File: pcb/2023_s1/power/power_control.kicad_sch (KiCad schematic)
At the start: 21 parts, among them J1 Conn_01x05_Male, Q2 TIP122, U1 40106, U3 4N25

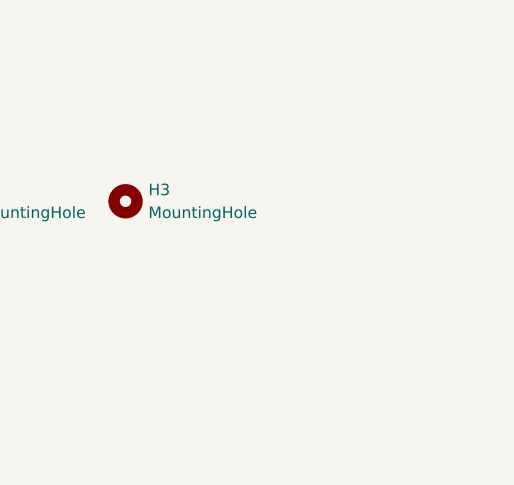
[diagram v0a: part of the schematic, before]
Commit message: fix, added a 4th mounting hole and rerouted the pcb in order to make feasible to solder given our poor infrastructure for PCB production
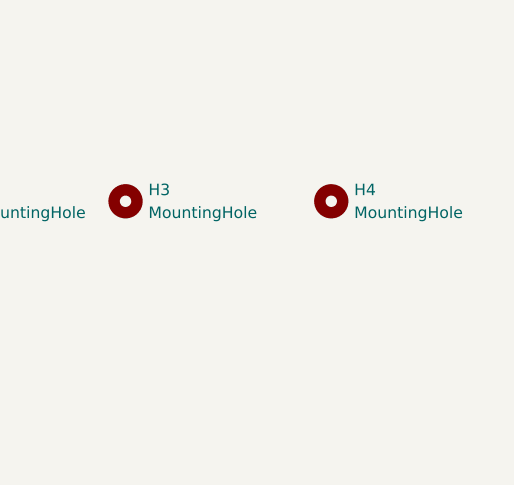
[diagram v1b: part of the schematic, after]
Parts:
- added H4: MountingHole, MountingHole:MountingHole_3.2mm_M3_DIN965_Pad, symbol Mechanical:MountingHole
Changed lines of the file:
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@@
     (pin "3")
+  )
+  (symbol (lib_id "Mechanical:MountingHole") (at 204.47 33.02 0) (unit 1)
+    (in_bom yes) (on_board yes) (fields_autoplaced)
+    (property "Reference" "H4" (id 0) (at 207.01 31.7499 0)
+      (effects (font (size 1.27 1.27)) (justify left))
+    )
+    (property "Value" "MountingHole" (id 1) (at 207.01 34.2899 0)
+      (effects (font (size 1.27 1.27)) (justify left))
+    )
+    (property "Footprint" "MountingHole:MountingHole_3.2mm_M3_DIN965_Pad" (id 2) (at 204.47 33.02 0)
+      (effects (font (size 1.27 1.27)) hide)
+    )
+    (property "Datasheet" "~" (id 3) (at 204.47 33.02 0)
+      (effects (font (size 1.27 1.27)) hide)
+    )
   )
   (symbol (lib_id "Connector:Screw_Terminal_01x02") (at 94.996 41.021 0) (unit 1)
@@
       (reference "H3") (unit 1) (value "MountingHole") (footprint "MountingHole:MountingHole_3.2mm_M3_DIN965_Pad")
     )
+    (path "/613046ba-2470-4560-9474-2ccc8166422c"
+      (reference "H4") (unit 1) (value "MountingHole") (footprint "MountingHole:MountingHole_3.2mm_M3_DIN965_Pad")
+    )
     (path "/656d544d-84ad-4bbf-8e72-6258e93c8b6e"

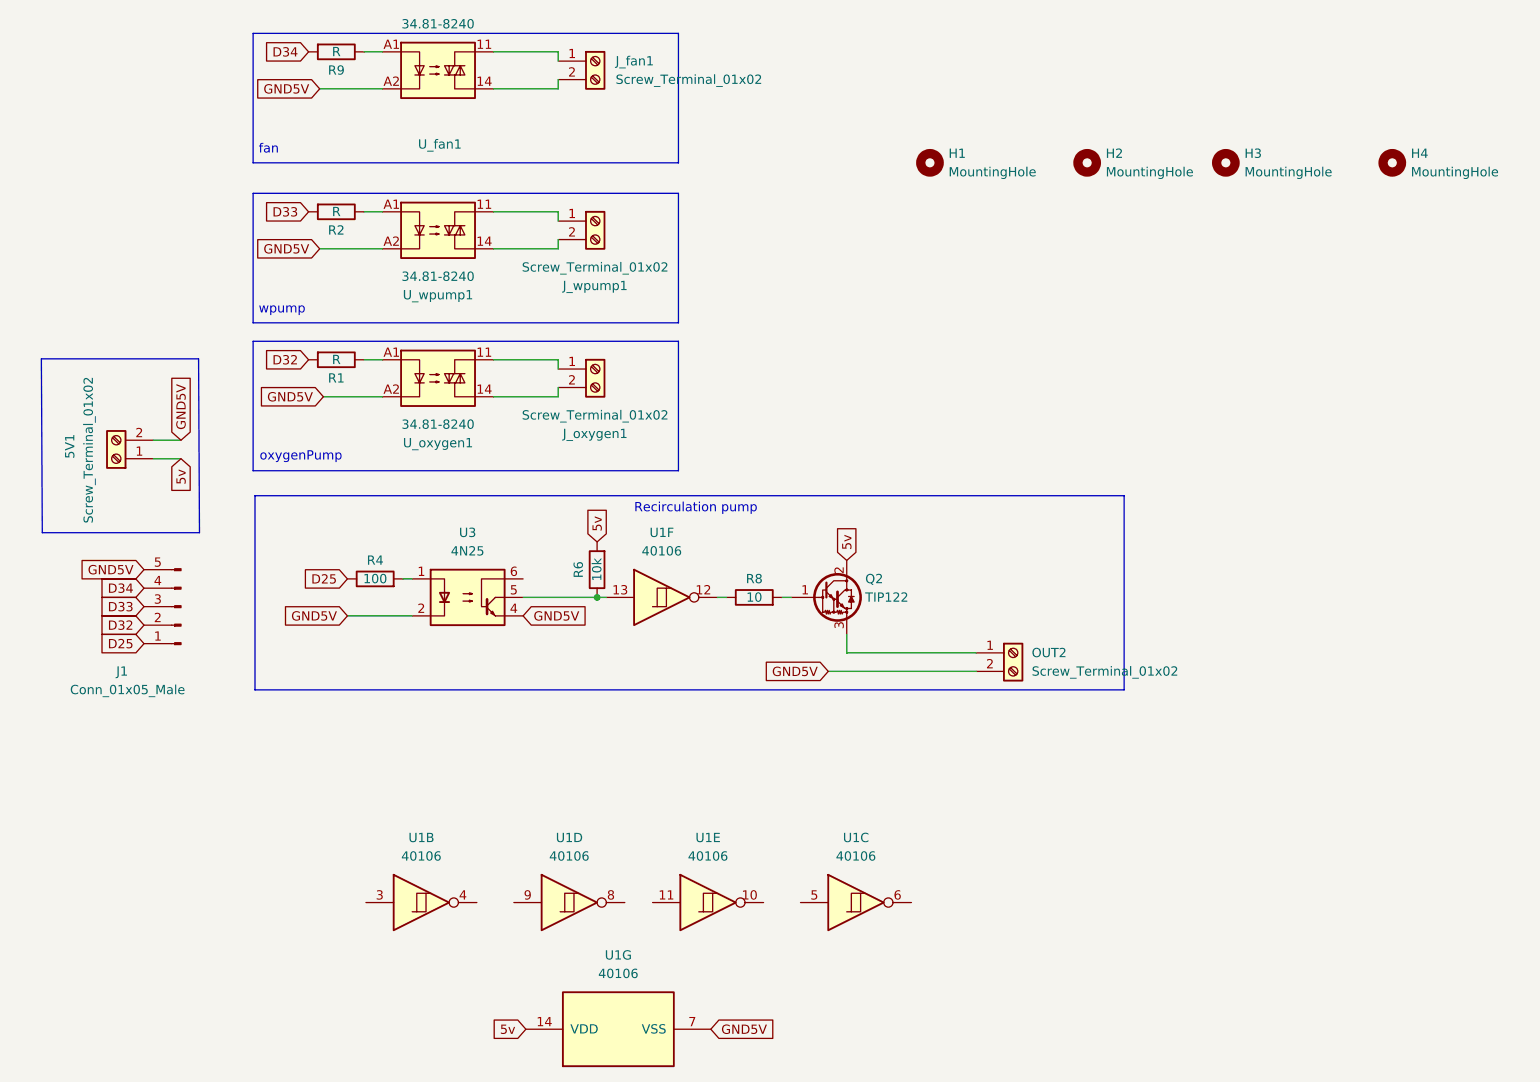
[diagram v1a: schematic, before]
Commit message: update, reselection of output pins and ds18b20 pin, rerouting and resizing of pads
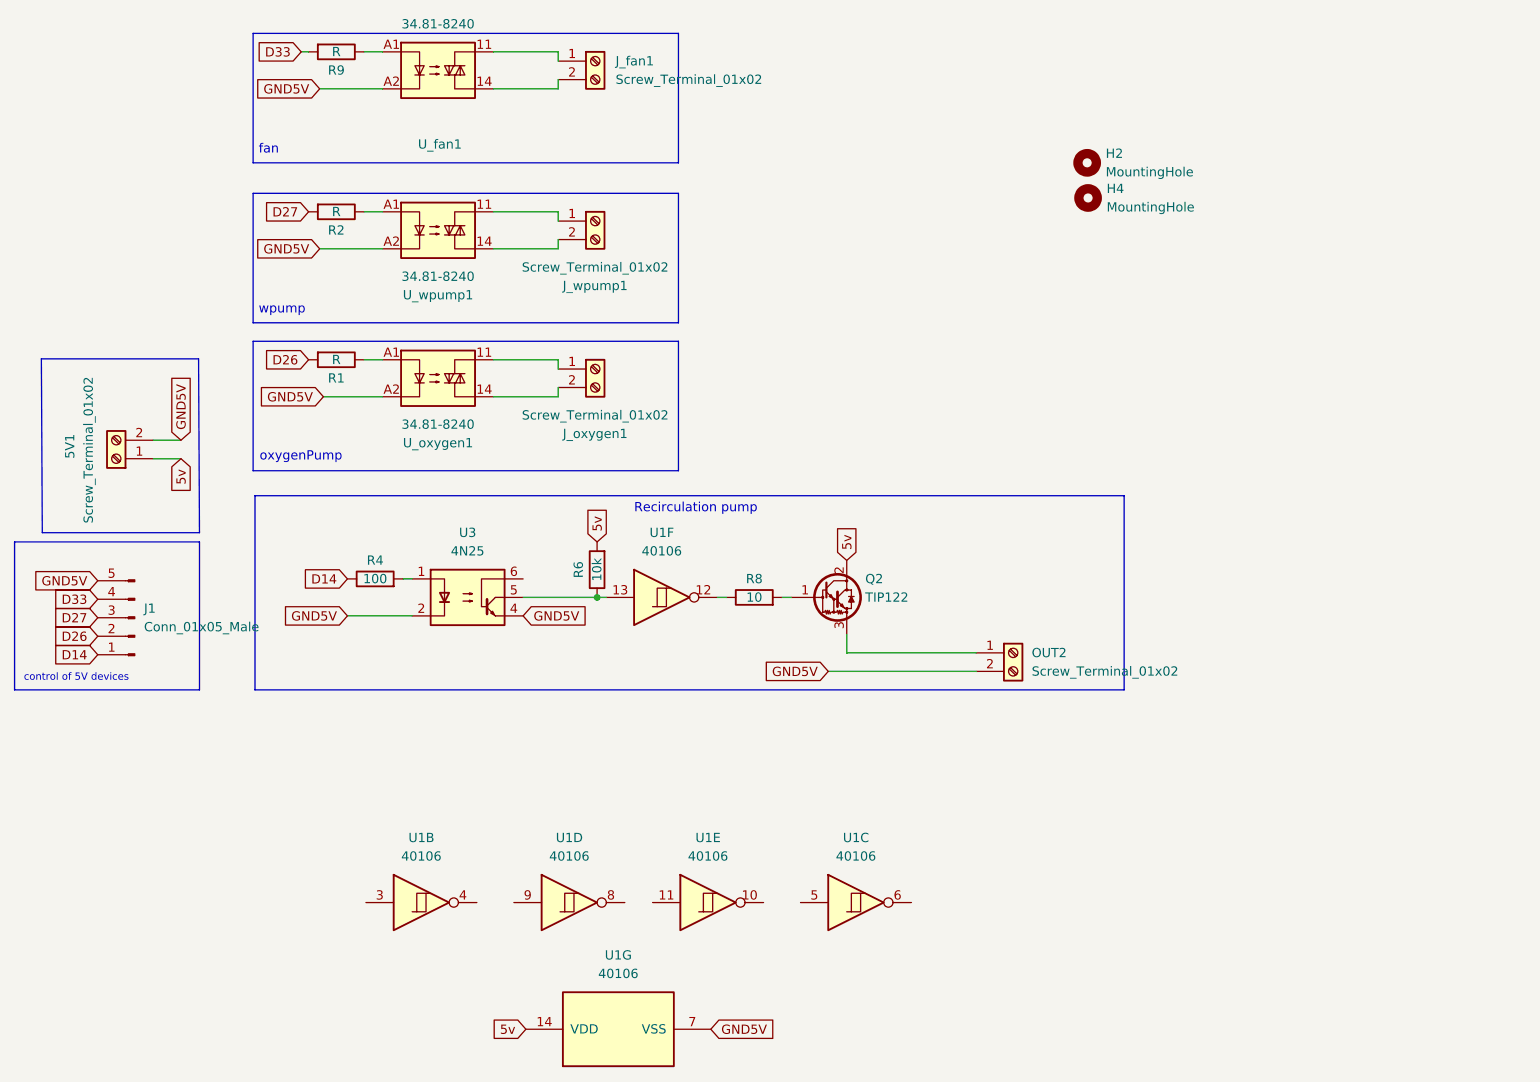
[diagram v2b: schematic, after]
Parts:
- removed H1, H3: MountingHole, MountingHole:MountingHole_3.2mm_M3_DIN965_Pad, symbol Mechanical:MountingHole
- U_fan1, U_oxygen1, U_wpump1: footprint OptoDevice:Finder_34.81 -> smart_sensor:G3MB-202P
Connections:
- net D34 is gone; now on net D33: J1.4 (Pin_4), R9.2
- net D33: no longer J1.3 (Pin_3), R2.2
- net D25 renamed D14
- net D32 renamed D26
- new net D27: J1.3 (Pin_3), R2.2
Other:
- note added: "control of 5V devices"
- moved on the sheet: H4

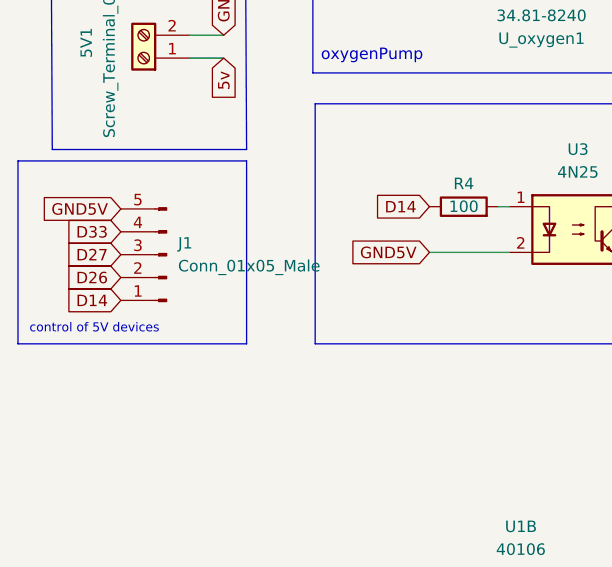
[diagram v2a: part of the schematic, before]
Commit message: update, changed some terminals to screw terminals for easyer connection
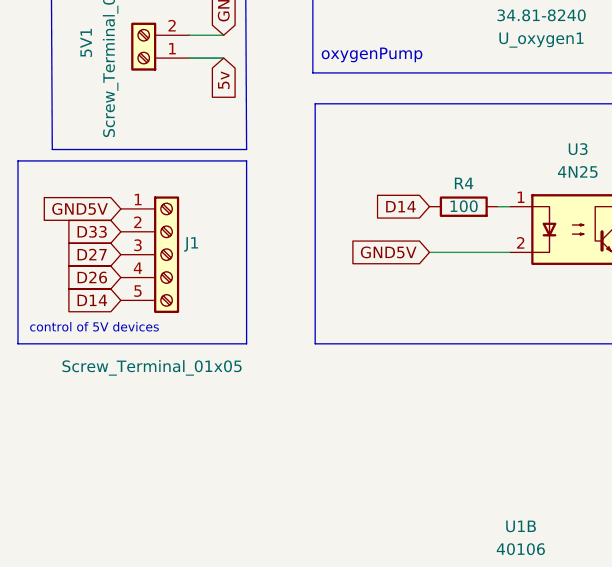
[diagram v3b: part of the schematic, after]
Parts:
- removed J1: Conn_01x05_Male, Connector_JST:JST_EH_B5B-EH-A_1x05_P2.50mm_Vertical, symbol Connector:Conn_01x05_Male
- added J1: Screw_Terminal_01x05, TerminalBlock_Altech:Altech_AK300_1x05_P5.00mm_45-Degree, symbol Connector:Screw_Terminal_01x05
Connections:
- net D14: now also J1.5 (Pin_5)
- net D26: now also J1.4 (Pin_4)
- net D27: now also J1.3 (Pin_3)
- net D33: now also J1.2 (Pin_2)
- net GND5V: now also J1.1 (Pin_1)
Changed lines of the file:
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@@
     (pin "2")
-  )
-  (symbol (lib_id "Connector:Conn_01x05_Male") (at 31.75 95.504 180) (unit 1)
-    (in_bom yes) (on_board yes) (fields_autoplaced)
-    (property "Reference" "J1" (id 0) (at 33.02 94.2339 0)
-      (effects (font (size 1.27 1.27)) (justify right))
-    )
-    (property "Value" "Conn_01x05_Male" (id 1) (at 33.02 96.7739 0)
-      (effects (font (size 1.27 1.27)) (justify right))
-    )
-    (property "Footprint" "Connector_JST:JST_EH_B5B-EH-A_1x05_P2.50mm_Vertical" (id 2) (at 31.75 95.504 0)
-      (effects (font (size 1.27 1.27)) hide)
-    )
-    (property "Datasheet" "~" (id 3) (at 31.75 95.504 0)
-      (effects (font (size 1.27 1.27)) hide)
-    )
-    (pin "1")
-    (pin "2")
-    (pin "3")
-    (pin "4")
-    (pin "5")
   )
   (symbol (lib_id "4xxx:40106") (at 104.14 92.71 0) (unit 6)
@@
     (pin "2")
   )
+  (symbol (lib_id "Connector:Screw_Terminal_01x05") (at 31.75 95.504 0) (unit 1)
+    (in_bom yes) (on_board yes)
+    (property "Reference" "J1" (id 0) (at 33.782 94.2339 0)
+      (effects (font (size 1.27 1.27)) (justify left))
+    )
+    (property "Value" "Screw_Terminal_01x05" (id 1) (at 20.066 107.95 0)
+      (effects (font (size 1.27 1.27)) (justify left))
+    )
+    (property "Footprint" "TerminalBlock_Altech:Altech_AK300_1x05_P5.00mm_45-Degree" (id 2) (at 31.75 95.504 0)
+      (effects (font (size 1.27 1.27)) hide)
+    )
+    (property "Datasheet" "~" (id 3) (at 31.75 95.504 0)
+      (effects (font (size 1.27 1.27)) hide)
+    )
+    (pin "1")
+    (pin "2")
+    (pin "3")
+    (pin "4")
+    (pin "5")
+  )
   (symbol (lib_id "Connector:Screw_Terminal_01x02") (at 94.996 61.341 0) (unit 1)
     (in_bom yes) (on_board yes) (fields_autoplaced)
@@
       (reference "H4") (unit 1) (value "MountingHole") (footprint "MountingHole:MountingHole_3.2mm_M3_DIN965_Pad")
     )
-    (path "/1fe06df7-d0ef-4823-aade-ee9d2f7c4e5a"
-      (reference "J1") (unit 1) (value "Conn_01x05_Male") (footprint "Connector_JST:JST_EH_B5B-EH-A_1x05_P2.50mm_Vertical")
+    (path "/d65748cd-df03-49d9-b201-cc9fd62ec626"
+      (reference "J1") (unit 1) (value "Screw_Terminal_01x05") (footprint "TerminalBlock_Altech:Altech_AK300_1x05_P5.00mm_45-Degree")
     )
     (path "/e91da800-d88c-49fe-a308-505fbb7061c1"

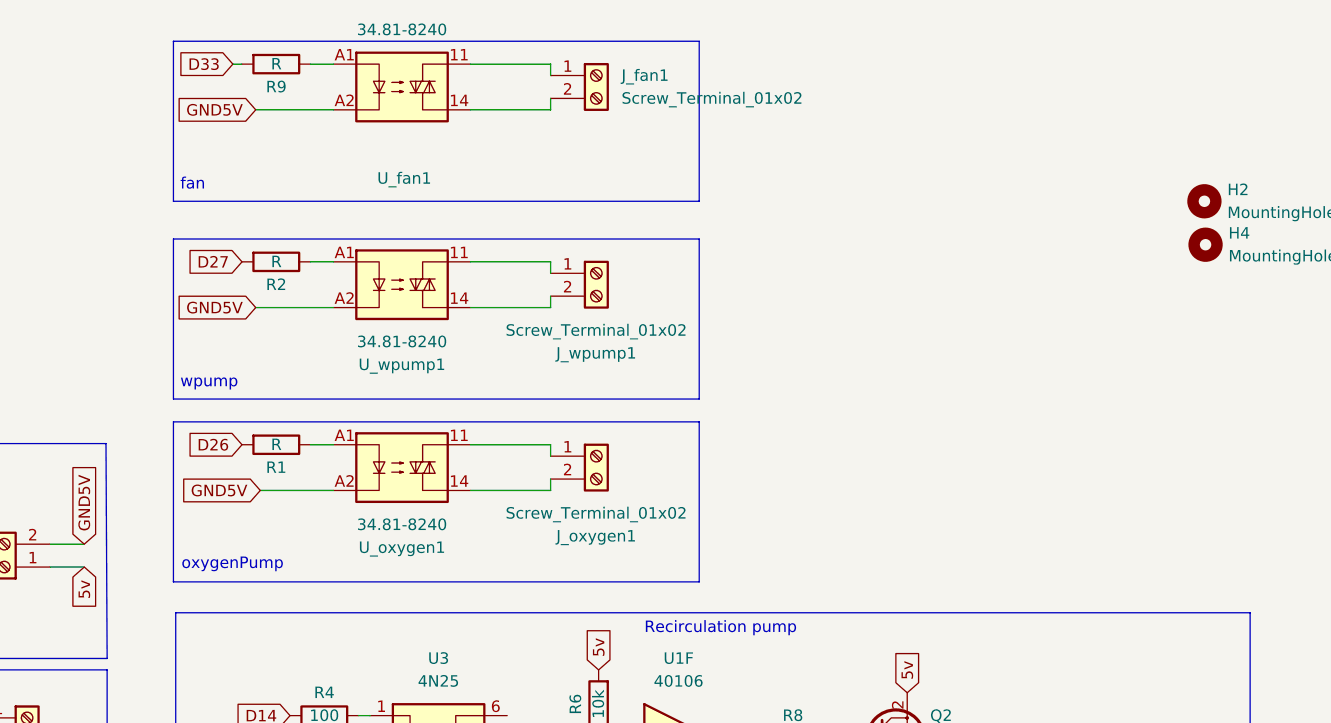
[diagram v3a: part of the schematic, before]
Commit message: update, based on experience and practice connecting AC devices proposed a change to the pcb, to make it easier to connect, and more intuitive
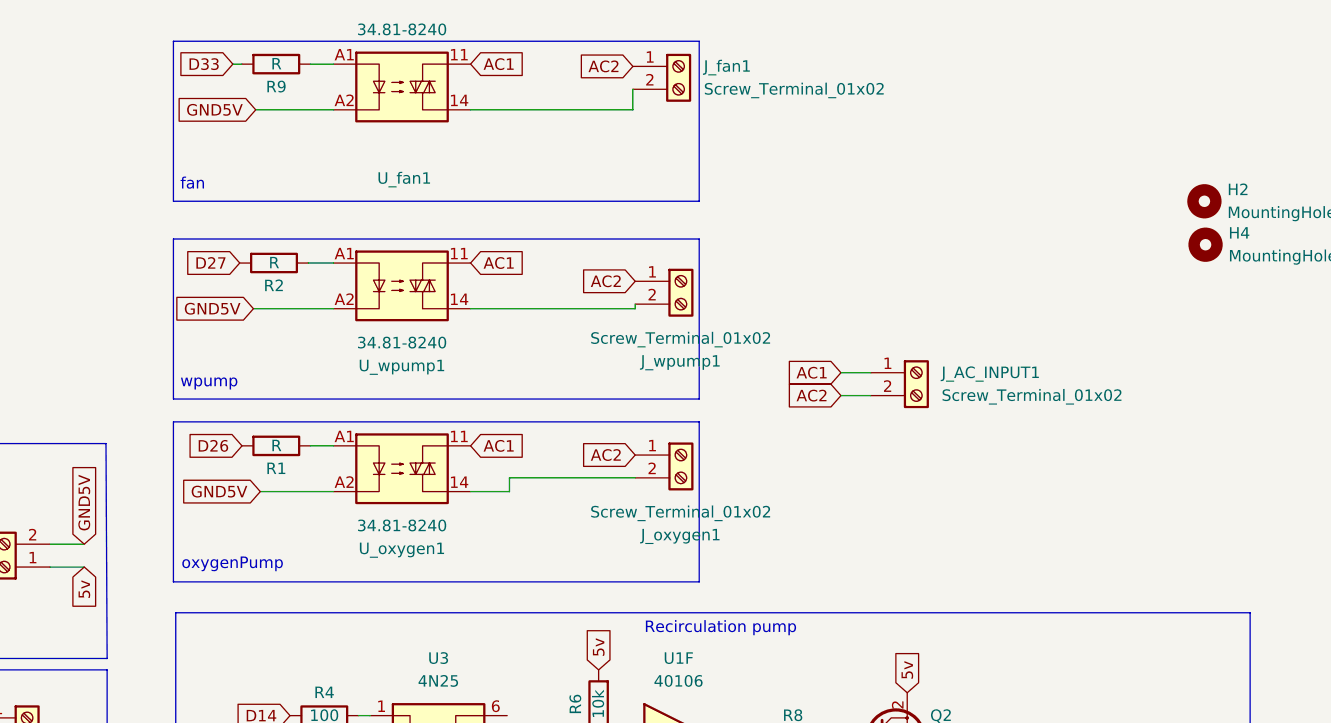
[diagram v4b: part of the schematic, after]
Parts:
- added J_AC_INPUT1: Screw_Terminal_01x02, TerminalBlock:TerminalBlock_Altech_AK300-2_P5.00mm, symbol Connector:Screw_Terminal_01x02
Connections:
- net AC1: now reaches U_wpump1.11
- net AC1: now also U_fan1.11, U_oxygen1.11, J_AC_INPUT1.1 (Pin_1); no longer J_wpump1.1 (Pin_1)
- net AC2: now reaches J_oxygen1.1 (Pin_1)
- net AC2: now also J_fan1.1 (Pin_1), J_wpump1.1 (Pin_1), J_AC_INPUT1.2 (Pin_2); no longer U_oxygen1.11
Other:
- moved on the sheet: J_fan1, J_oxygen1, J_wpump1
